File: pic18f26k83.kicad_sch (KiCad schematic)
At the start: 20 parts, among them IC1 PIC18F26K83-I_SO, SW1 TL3305AF260QG, Y2 ECS-80-20-5PX-TR

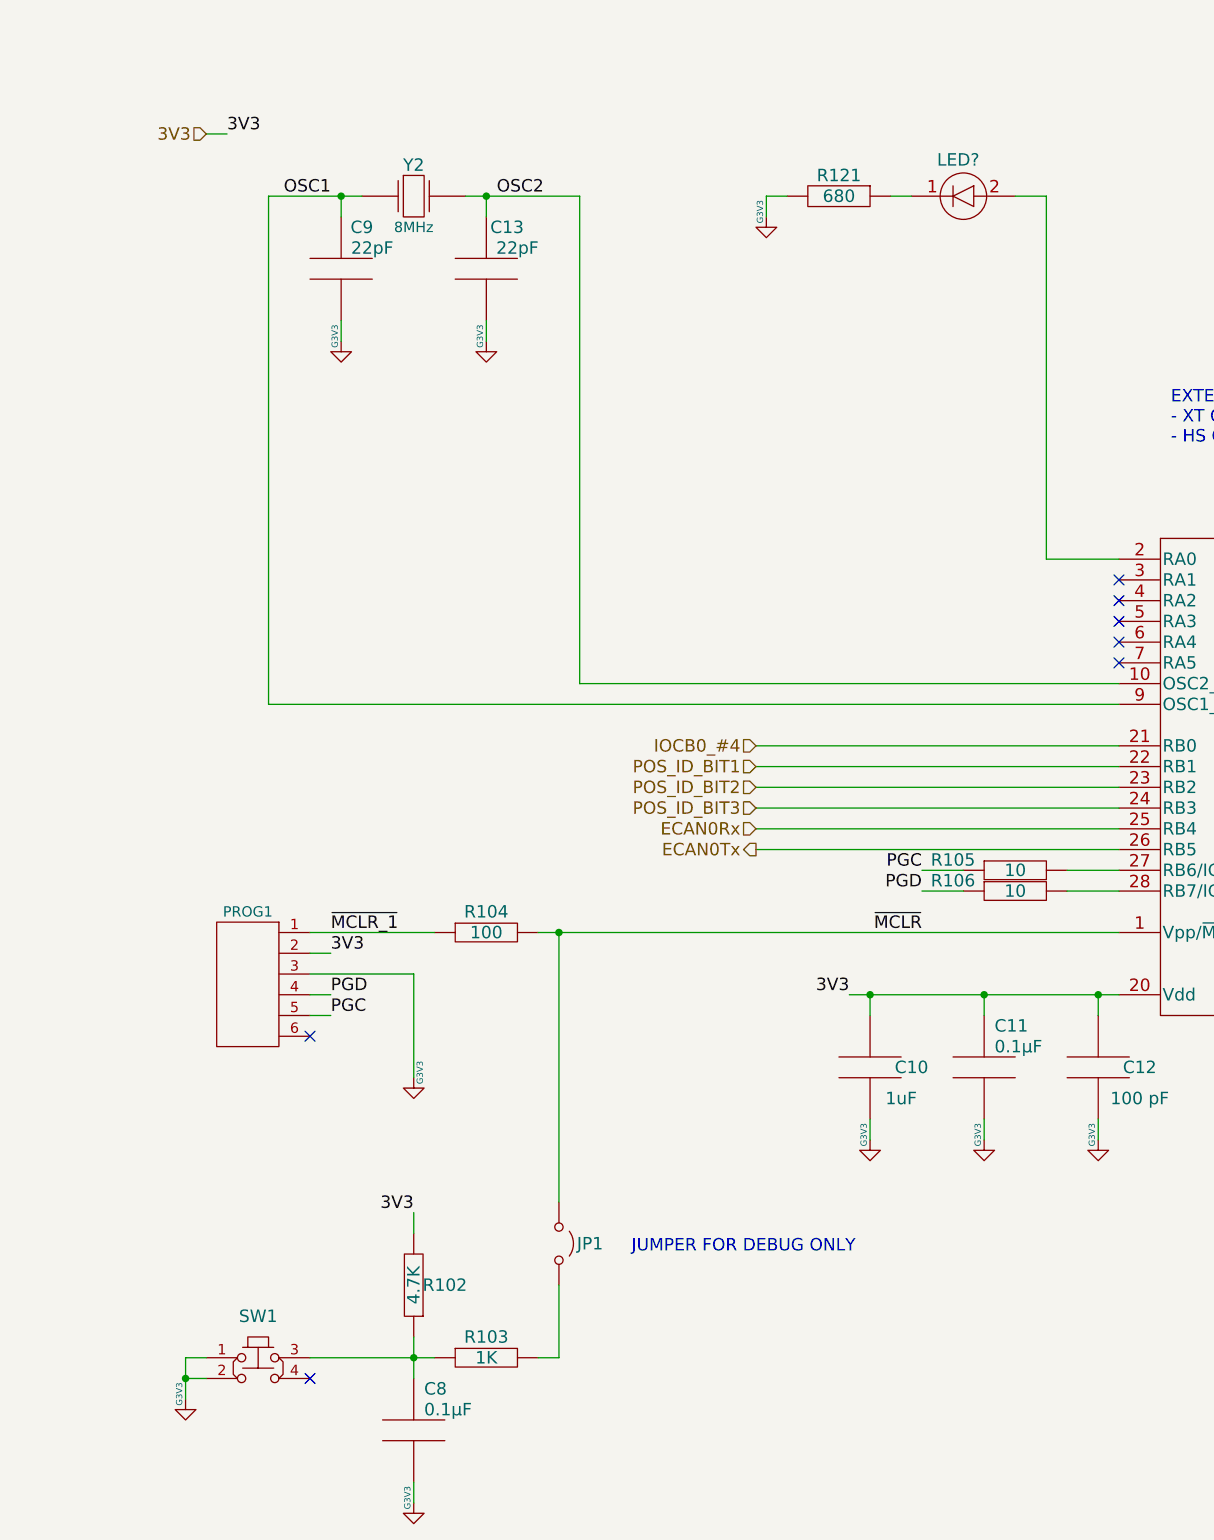
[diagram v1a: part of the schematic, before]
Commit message: kicad 9 - r11-check gerber before sending to manufacturing
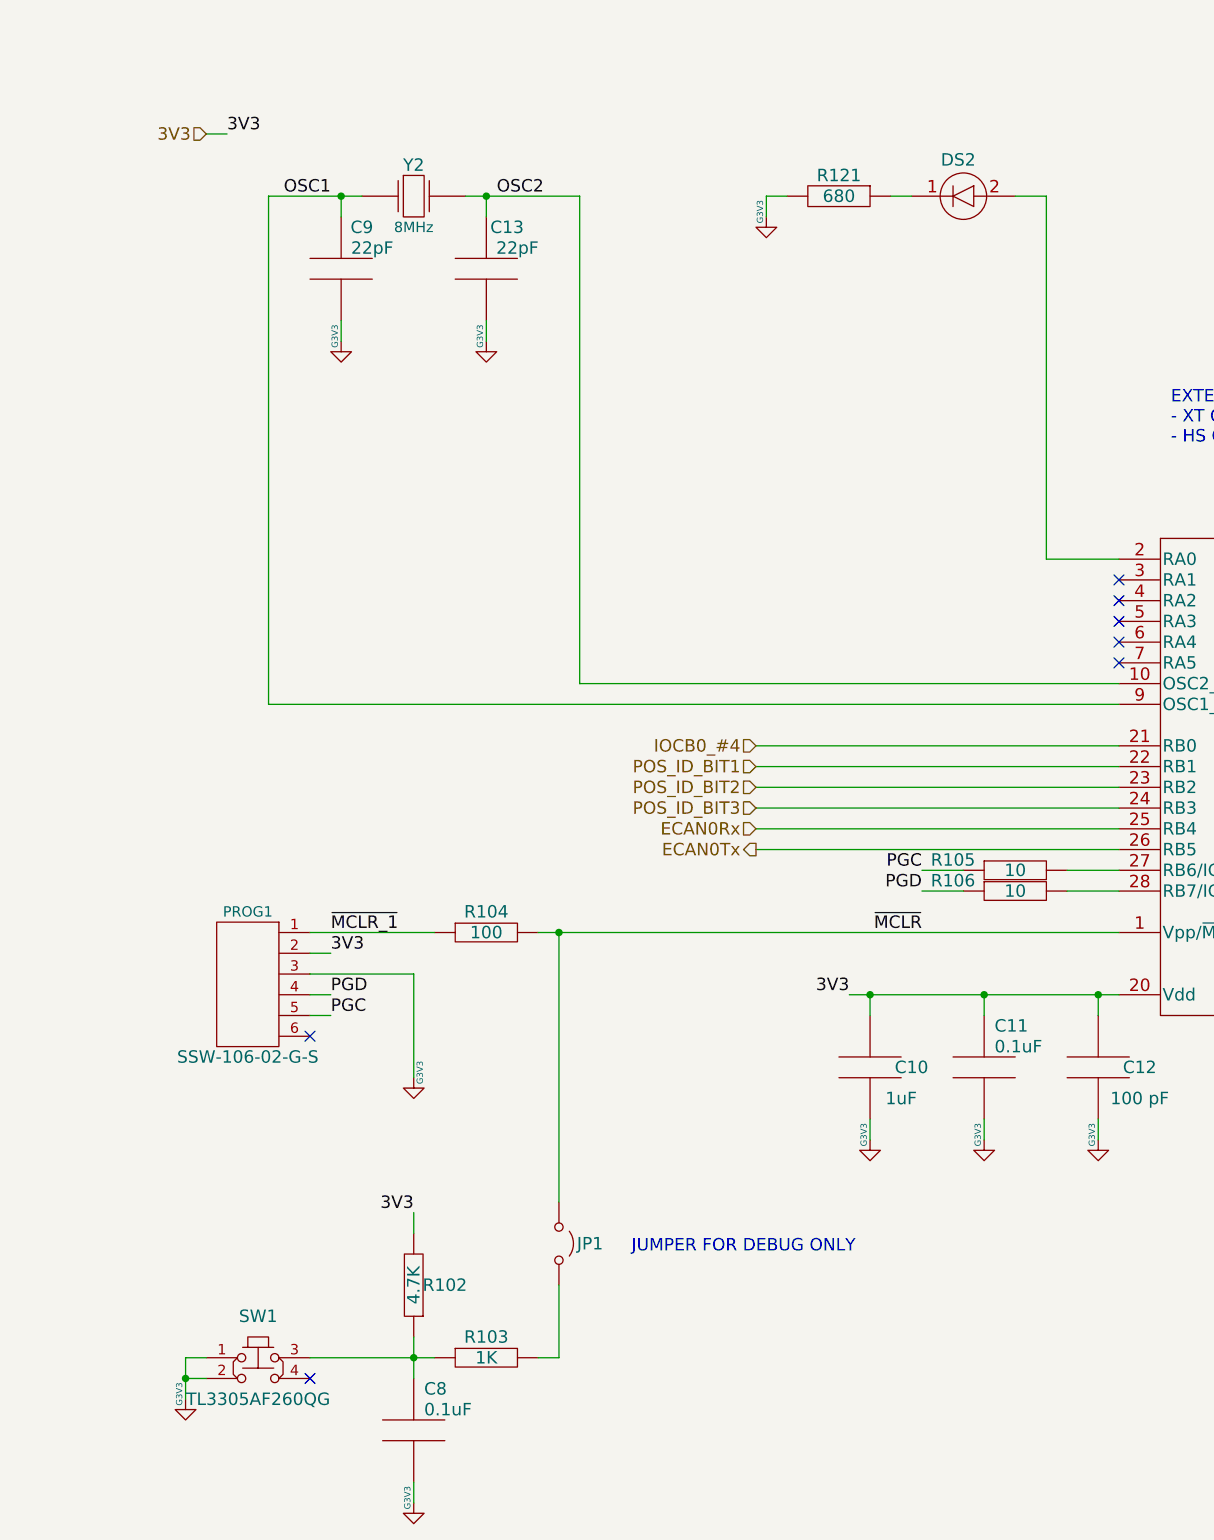
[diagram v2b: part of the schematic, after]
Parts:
- C10: SupllierPartNumber 478-7956-1-ND -> (none)
- C11, C8: Nominal 0.1µF -> 0.1uF; SupllierPartNumber 478-3352-1-ND -> (none)
- C12: SupllierPartNumber 399-7981-1-ND -> (none)
- IC1: SupllierPartNumber PIC18F26K83-I/SO-ND -> (none)
- JP1: SupllierPartNumber 732-5315-ND -> (none)
- PROG1: SupllierPartNumber SAM1225-06-ND -> (none); SupplierDevicePackage Through Hole -> (none)
- R102: SupllierPartNumber 311-4.7KARCT-ND -> (none); Tolerance 5% -> (none)
- R103: SupllierPartNumber 311-1.00KCRCT-ND -> (none); Tolerance 1% -> (none)
- R104: SupllierPartNumber 311-100CRCT-ND -> (none)
- R105, R106: SupllierPartNumber 311-10.0CRCT-ND -> (none)
- R115, R116: SupllierPartNumber 311-0.0ARCT-ND -> (none)
- R121: SupllierPartNumber RMCF0805JT680RCT-ND -> (none)
- Y2: SupllierPartNumber XC2076CT-ND -> (none)
- gave numbers to parts that had none: 1
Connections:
- net GNDD renamed GND_3V3

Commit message: r11a - clean up mostly with reports naming, values, footprints and parts
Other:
- company: ARXTRON TECHNOLOGIES -> ${COMPANY}
- title: EOL ECU MIX CARD -> ${PART_NUM} ${PCB_NAME} ${ASSY_VARIANT} ${ASSY_NAME}
- moved on the sheet: PROG1
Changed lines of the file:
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@@
 	(paper "A3")
 	(title_block
-		(title "EOL ECU MIX CARD")
-		(date "2023-09-26")
-		(rev "0C")
-		(company "ARXTRON TECHNOLOGIES")
-		(comment 1 "A0180-V0")
-		(comment 2 "PRJ22180")
-		(comment 3 "EOL ECU RCM8 RCM9")
-		(comment 4 "ANTON TOKARSKYI")
+		(title "${PART_NUM} ${PCB_NAME} ${ASSY_VARIANT} ${ASSY_NAME}")
+		(date "2025-03-12")
+		(rev "${REVISION}${REVISION_SCH}")
+		(company "${COMPANY}")
+		(comment 1 "${PART_NUM}")
+		(comment 2 "${PRJ_NUM}")
+		(comment 3 "${PRJ_NAME}")
+		(comment 4 "${DESIGNED}")
+		(comment 5 "${PART_NUM_ICT}")
 	)
 	(text "EXTERNAL CLOCK SOURCE:\n- XT Oscillator mode\n- HS Oscillator mode"
@@
 	(symbol
 		(lib_id "Connector_Samtec:SSW-106-02-G-S")
-		(at 43.18 146.05 0)
-		(mirror y)
+		(at 46.99 140.97 0)
 		(unit 1)
 		(exclude_from_sim no)
@@
 		(dnp no)
 		(property "Reference" "PROG1"
-			(at 39.37 138.43 0)
+			(at 39.37 137.16 0)
 			(effects
 				(font
@@
 		)
 		(property "Value" "SSW-106-02-G-S"
-			(at 39.37 166.37 0)
+			(at 50.8 161.29 0)
 			(effects
 				(font
@@
 		)
 		(property "Footprint" "_Connector_Samtec:SAMTEC_SSW-106-02-G-S"
-			(at 39.37 173.99 0)
+			(at 50.8 168.91 0)
 			(effects
 				(font
@@
 		)
 		(property "Datasheet" ""
-			(at 41.91 146.05 0)
+			(at 48.26 140.97 0)
 			(effects
 				(font
@@
 		)
 		(property "Description" "CONN HDR 6POS 0.1 GOLD PCB"
-			(at 39.37 161.29 0)
+			(at 50.8 156.21 0)
 			(effects
 				(font
@@
 		)
 		(property "ManufacturerPartNumber" "SSW-106-02-G-S"
-			(at 39.37 156.21 0)
+			(at 50.8 151.13 0)
 			(effects
 				(font
 					(size 1.524 1.524)
 				)
+				(hide yes)
 			)
 		)
 		(property "Supplier" "Samtec Inc."
-			(at 39.37 171.45 0)
+			(at 50.8 166.37 0)
 			(effects
 				(font
@@
 		)
 		(property "Manufacturer" "Samtec Inc."
-			(at 38.1 163.83 0)
+			(at 52.07 158.75 0)
 			(effects
 				(font
@@
 		)
 		(property "SupplierPartNumber" "SSW-106-02-G-S"
-			(at 39.37 158.75 0)
+			(at 50.8 153.67 0)
 			(effects
 				(font
